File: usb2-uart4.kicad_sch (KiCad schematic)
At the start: 28 parts, among them U1 CH344Q, U13 TPNUP2202W1T2G, X1 ASV-xxxMHz, Y1 8MHz

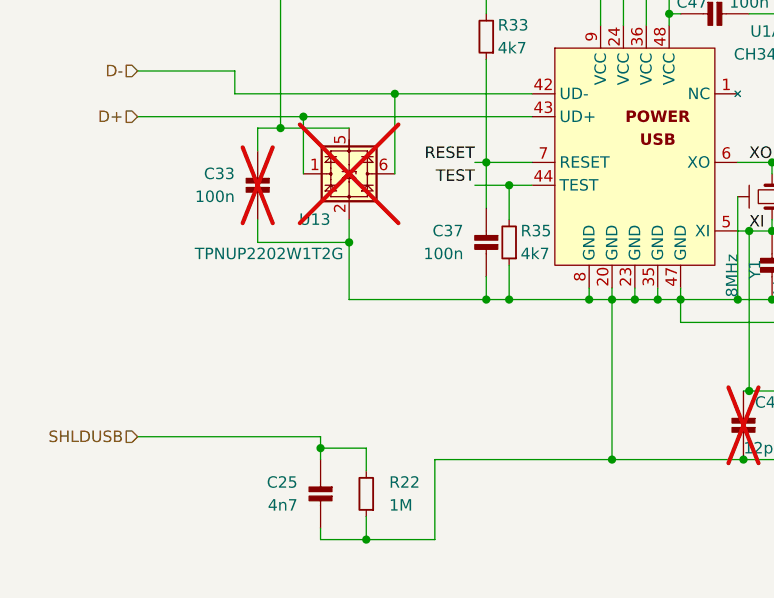
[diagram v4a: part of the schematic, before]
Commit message: H_passives:CAP_NP -> isouart4:CAP_NP
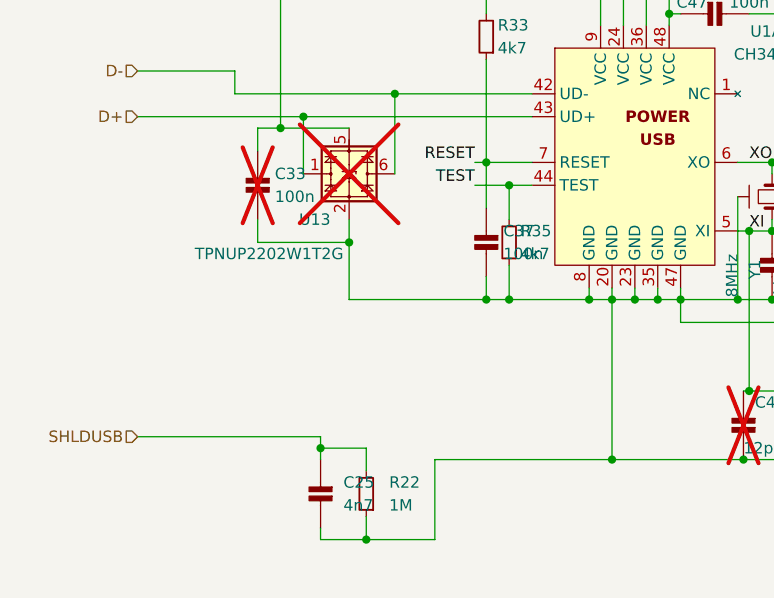
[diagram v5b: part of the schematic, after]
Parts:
- C25, C37, C47, C48, C50: footprint Capacitor_SMD:C_0805_2012Metric_Pad1.18x1.45mm_HandSolder -> Capacitor_SMD:C_0603_1608Metric_Pad1.08x0.95mm_HandSolder; symbol H_passives:CAP_NP -> isouart4:CAP_NP
- C33: symbol H_passives:CAP_NP -> isouart4:CAP_NP; now in the parts list
- C44, C45, C46, C47: symbol H_passives:CAP_NP -> isouart4:CAP_NP
- C47, C48: footprint Capacitor_SMD:C_0805_2012Metric_Pad1.18x1.45mm_HandSolder -> Capacitor_SMD:C_0603_1608Metric_Pad1.08x0.95mm_HandSolder; symbol H_passives:CAP_NP -> isouart4:CAP_NP; now in the parts list
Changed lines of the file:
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@@
     (effects (font (size 1.27 1.27)) (justify left))
   )
-  (symbol (lib_id "H_passives:CAP_NP") (at 127.635 85.09 270) (unit 1)
+  (symbol (lib_id "isouart4:CAP_NP") (at 127.635 85.09 270) (unit 1)
     (in_bom yes) (on_board yes) (dnp no)
     (property "Reference" "C45" (at 125.095 83.82 90)
@@
     )
   )
-  (symbol (lib_id "H_passives:CAP_NP") (at 83.82 146.05 180) (unit 1)
+  (symbol (lib_id "isouart4:CAP_NP") (at 83.82 146.05 180) (unit 1)
     (in_bom yes) (on_board yes) (dnp no) (fields_autoplaced)
-    (property "Reference" "C25" (at 81.28 144.7799 0)
-      (effects (font (size 1.27 1.27)) (justify left))
-    )
-    (property "Value" "4n7" (at 81.28 147.3199 0)
-      (effects (font (size 1.27 1.27)) (justify left))
-    )
-    (property "Footprint" "Capacitor_SMD:C_0805_2012Metric_Pad1.18x1.45mm_HandSolder" (at 83.82 144.78 0)
+    (property "Reference" "C25" (at 86.36 144.78 0)
+      (effects (font (size 1.27 1.27)) (justify right))
+    )
+    (property "Value" "4n7" (at 86.36 147.32 0)
+      (effects (font (size 1.27 1.27)) (justify right))
+    )
+    (property "Footprint" "Capacitor_SMD:C_0603_1608Metric_Pad1.08x0.95mm_HandSolder" (at 83.82 144.78 0)
       (effects (font (size 1.27 1.27)) hide)
     )
@@
     )
   )
-  (symbol (lib_id "H_passives:CAP_NP") (at 102.235 118.11 180) (unit 1)
+  (symbol (lib_id "isouart4:CAP_NP") (at 102.235 118.11 180) (unit 1)
     (in_bom yes) (on_board yes) (dnp no) (fields_autoplaced)
-    (property "Reference" "C37" (at 99.695 116.8399 0)
-      (effects (font (size 1.27 1.27)) (justify left))
-    )
-    (property "Value" "100n" (at 99.695 119.3799 0)
-      (effects (font (size 1.27 1.27)) (justify left))
-    )
-    (property "Footprint" "Capacitor_SMD:C_0805_2012Metric_Pad1.18x1.45mm_HandSolder" (at 102.235 116.84 0)
+    (property "Reference" "C37" (at 104.14 116.84 0)
+      (effects (font (size 1.27 1.27)) (justify right))
+    )
+    (property "Value" "100n" (at 104.14 119.38 0)
+      (effects (font (size 1.27 1.27)) (justify right))
+    )
+    (property "Footprint" "Capacitor_SMD:C_0603_1608Metric_Pad1.08x0.95mm_HandSolder" (at 102.235 116.84 0)
       (effects (font (size 1.27 1.27)) hide)
     )
@@
     )
   )
-  (symbol (lib_id "H_passives:CAP_NP") (at 158.75 120.015 270) (unit 1)
-    (in_bom no) (on_board no) (dnp yes)
+  (symbol (lib_id "isouart4:CAP_NP") (at 158.75 120.015 270) (unit 1)
+    (in_bom yes) (on_board yes) (dnp yes)
     (property "Reference" "C47" (at 156.21 118.745 90)
       (effects (font (size 1.27 1.27)))
@@
       (effects (font (size 1.27 1.27)))
     )
-    (property "Footprint" "Capacitor_SMD:C_0805_2012Metric_Pad1.18x1.45mm_HandSolder" (at 157.48 120.015 0)
+    (property "Footprint" "Capacitor_SMD:C_0603_1608Metric_Pad1.08x0.95mm_HandSolder" (at 157.48 120.015 0)
       (effects (font (size 1.27 1.27)) hide)
     )
@@
     )
   )
-  (symbol (lib_id "H_passives:CAP_NP") (at 130.81 138.43 180) (unit 1)
-    (in_bom no) (on_board no) (dnp yes)
+  (symbol (lib_id "isouart4:CAP_NP") (at 130.81 138.43 180) (unit 1)
+    (in_bom yes) (on_board yes) (dnp yes)
     (property "Reference" "C48" (at 132.08 135.89 0)
       (effects (font (size 1.27 1.27)) (justify right))
@@
       (effects (font (size 1.27 1.27)) (justify right))
     )
-    (property "Footprint" "Capacitor_SMD:C_0805_2012Metric_Pad1.18x1.45mm_HandSolder" (at 130.81 137.16 0)
+    (property "Footprint" "Capacitor_SMD:C_0603_1608Metric_Pad1.08x0.95mm_HandSolder" (at 130.81 137.16 0)
       (effects (font (size 1.27 1.27)) hide)
     )
@@
     )
   )
-  (symbol (lib_id "H_passives:CAP_NP") (at 69.215 22.225 0) (unit 1)
+  (symbol (lib_id "isouart4:CAP_NP") (at 69.215 22.225 0) (unit 1)
     (in_bom yes) (on_board yes) (dnp no)
     (property "Reference" "C47" (at 67.945 24.765 90)
@@
       (effects (font (size 1.27 1.27)))
     )
-    (property "Footprint" "Capacitor_SMD:C_0805_2012Metric_Pad1.18x1.45mm_HandSolder" (at 69.215 23.495 0)
+    (property "Footprint" "Capacitor_SMD:C_0603_1608Metric_Pad1.08x0.95mm_HandSolder" (at 69.215 23.495 0)
       (effects (font (size 1.27 1.27)) hide)
     )
@@
     )
   )
-  (symbol (lib_id "H_passives:CAP_NP") (at 144.145 120.65 180) (unit 1)
+  (symbol (lib_id "isouart4:CAP_NP") (at 144.145 120.65 180) (unit 1)
     (in_bom yes) (on_board yes) (dnp no)
     (property "Reference" "C50" (at 140.335 118.11 0)
@@
       (effects (font (size 1.27 1.27)) (justify right))
     )
-    (property "Footprint" "Capacitor_SMD:C_0805_2012Metric_Pad1.18x1.45mm_HandSolder" (at 144.145 119.38 0)
+    (property "Footprint" "Capacitor_SMD:C_0603_1608Metric_Pad1.08x0.95mm_HandSolder" (at 144.145 119.38 0)
       (effects (font (size 1.27 1.27)) hide)
     )
@@
     )
   )
-  (symbol (lib_id "H_passives:CAP_NP") (at 127.635 81.28 270) (unit 1)
+  (symbol (lib_id "isouart4:CAP_NP") (at 127.635 81.28 270) (unit 1)
     (in_bom yes) (on_board yes) (dnp no)
     (property "Reference" "C44" (at 125.095 80.01 90)
@@
     )
   )
-  (symbol (lib_id "H_passives:CAP_NP") (at 127.635 88.9 270) (unit 1)
+  (symbol (lib_id "isouart4:CAP_NP") (at 127.635 88.9 270) (unit 1)
     (in_bom yes) (on_board yes) (dnp no)
     (property "Reference" "C46" (at 125.095 87.63 90)
@@
     )
   )
-  (symbol (lib_id "H_passives:CAP_NP") (at 127.635 92.71 270) (unit 1)
+  (symbol (lib_id "isouart4:CAP_NP") (at 127.635 92.71 270) (unit 1)
     (in_bom yes) (on_board yes) (dnp no)
     (property "Reference" "C47" (at 125.095 91.44 90)
@@
     )
   )
-  (symbol (lib_id "H_passives:CAP_NP") (at 76.835 111.76 180) (unit 1)
-    (in_bom no) (on_board no) (dnp yes) (fields_autoplaced)
-    (property "Reference" "C33" (at 74.295 110.4899 0)
-      (effects (font (size 1.27 1.27)) (justify left))
-    )
-    (property "Value" "100n" (at 74.295 113.0299 0)
-      (effects (font (size 1.27 1.27)) (justify left))
+  (symbol (lib_id "isouart4:CAP_NP") (at 76.835 111.76 180) (unit 1)
+    (in_bom yes) (on_board yes) (dnp yes) (fields_autoplaced)
+    (property "Reference" "C33" (at 78.74 110.49 0)
+      (effects (font (size 1.27 1.27)) (justify right))
+    )
+    (property "Value" "100n" (at 78.74 113.03 0)
+      (effects (font (size 1.27 1.27)) (justify right))
     )
     (property "Footprint" "Capacitor_SMD:C_0603_1608Metric_Pad1.08x0.95mm_HandSolder" (at 76.835 110.49 0)
@@
     )
   )
-  (symbol (lib_id "H_passives:CAP_NP") (at 133.985 120.65 180) (unit 1)
+  (symbol (lib_id "isouart4:CAP_NP") (at 133.985 120.65 180) (unit 1)
     (in_bom yes) (on_board yes) (dnp no)
     (property "Reference" "C48" (at 135.255 118.11 0)
@@
       (effects (font (size 1.27 1.27)) (justify right))
     )
-    (property "Footprint" "Capacitor_SMD:C_0805_2012Metric_Pad1.18x1.45mm_HandSolder" (at 133.985 119.38 0)
-      (effects (font (size 1.27 1.27)) hide)
-    )
+    (property "Footprint" "Capacitor_SMD:C_0603_1608Metric_Pad1.08x0.95mm_HandSolder" (at 133.985 119.38 0)
+      (effects (font (size 1.27 1.27)) hide)
+    )

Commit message: Use the custom isouart4:Crystal_Small instead of Device:Crystal_Small
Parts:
- Y1: symbol Device:Crystal_Small -> isouart4:Crystal_Small
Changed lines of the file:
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@@
     )
   )
-  (symbol (lib_id "Device:Crystal_Small") (at 133.985 113.03 90) (unit 1)
+  (symbol (lib_id "isouart4:Crystal_Small") (at 133.985 113.03 90) (unit 1)
     (in_bom yes) (on_board yes) (dnp no)
     (property "Reference" "Y1" (at 132.08 120.015 0)

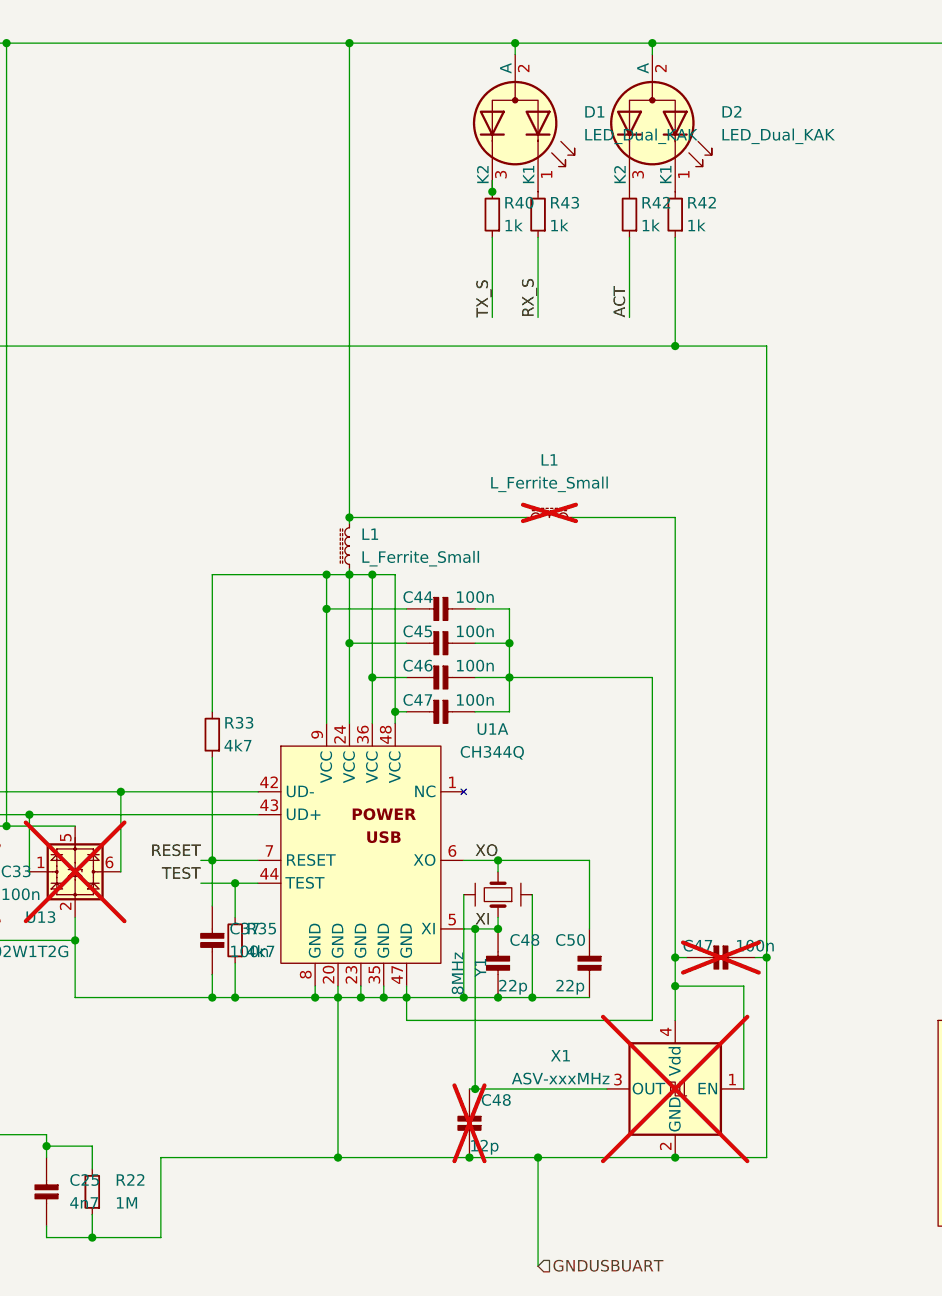
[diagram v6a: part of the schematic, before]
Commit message: remove X1
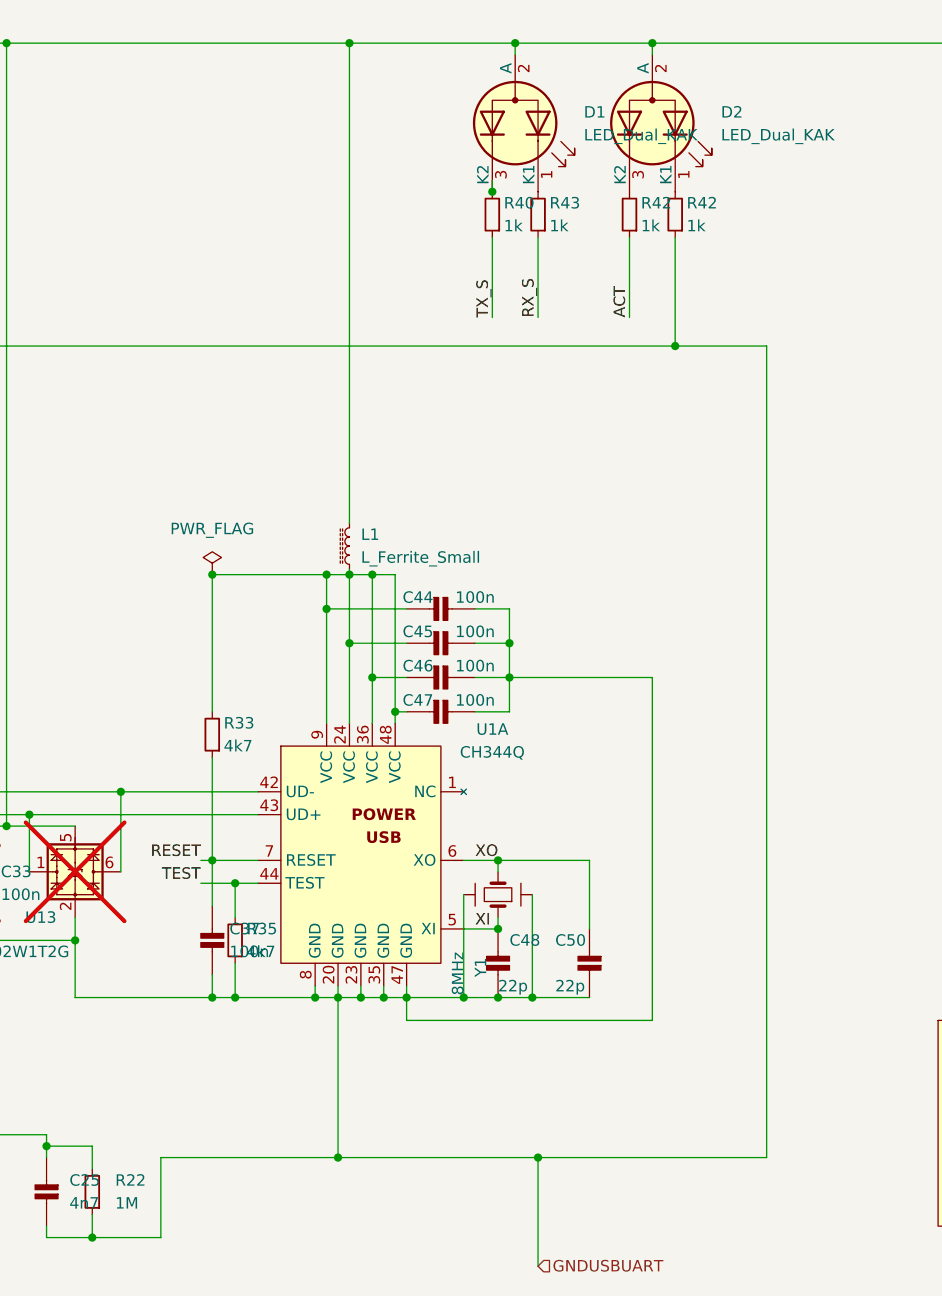
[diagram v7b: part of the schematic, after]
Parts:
- removed C47: 100n, Capacitor_SMD:C_0603_1608Metric_Pad1.08x0.95mm_HandSolder, symbol isouart4:CAP_NP
- removed C48: 12p, Capacitor_SMD:C_0603_1608Metric_Pad1.08x0.95mm_HandSolder, symbol isouart4:CAP_NP
- removed L1: L_Ferrite_Small, Inductor_SMD:L_TDK_NLV25_2.5x2.0mm, symbol Device:L_Ferrite_Small
- removed X1: ASV-xxxMHz, Oscillator:Oscillator_SMD_Abracon_ASV-4Pin_7.0x5.1mm, symbol Oscillator:ASV-xxxMHz
